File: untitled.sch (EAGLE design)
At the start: 62 parts, among them IC1 SIM900, IC2 ST1S10PHR, IC3 SMF05C, IC5 BQ24072, IC6 SIM68R, X1 ST-SMB-H, X2 ST-SMB-H

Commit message: Trace changes
Following items are changed:
- area between SIM900R and SIM68R footprints is restricted for placing
traces;
- some small changes in polygons around SIM900R;
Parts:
- removed R11: 22, rcl:R-EU_R0805
- removed SIM1: 912283001, con-molex-sim:912283001
- added JP10, JP11, JP12: (no value), pinhead:PINHD-1X1
- added SIM2: ICA-501, ICA-501:ICA-501
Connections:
- removed net N$15: IC3.5, R11.1, SIM1.PRESENCE
- net +4.8V: now also JP12.1
- net GND: now also SIM2.GND; no longer SIM1.GND
- net N$14: now also SIM2.RST; no longer SIM1.RST
- net N$17: now also SIM2.I/O; no longer SIM1.I/O
- net N$18: now also SIM2.CLK; no longer SIM1.CLK
- net SIM_PRESENCE: no longer R11.2
- net SIM_VDD: now also SIM2.VCC; no longer SIM1.VCC
- net VBAT: now also JP10.1, JP11.1
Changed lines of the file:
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@@
 <?xml version="1.0" encoding="utf-8"?>
 <!DOCTYPE eagle SYSTEM "eagle.dtd">
-<eagle version="6.4">
+<eagle version="6.5.0">
 <drawing>
 <settings>
@@
 <setting verticaltext="up"/>
 </settings>
-<grid distance="0.01" unitdist="inch" unit="inch" style="lines" multiple="1" display="no" altdistance="0.01" altunitdist="inch" altunit="inch"/>
+<grid distance="0.1" unitdist="inch" unit="inch" style="lines" multiple="1" display="no" altdistance="0.01" altunitdist="inch" altunit="inch"/>
 <layers>
 <layer number="1" name="Top" color="4" fill="1" visible="no" active="no"/>
@@
 <part name="R13" library="rcl" deviceset="R-EU_" device="R0805" value="22"/>
 <part name="R14" library="rcl" deviceset="R-EU_" device="R0805" value="22"/>
-<part name="R11" library="rcl" deviceset="R-EU_" device="R0805" value="22"/>
 <part name="VT3" library="transistor-npn" deviceset="MMBT3904" device=""/>
 <part name="GND24" library="supply1" deviceset="GND" device=""/>
@@
 <part name="R23" library="rcl" deviceset="R-EU_" device="R0805" value="4.7k"/>
 <part name="LED4" library="LED0805" deviceset="LED0805" device=""/>
-<part name="SIM1" library="con-molex-sim" deviceset="912283001" device=""/>
 <part name="IC6" library="sim68" deviceset="SIM68R" device=""/>
 <part name="SV2" library="con-lstb" deviceset="MA04-1" device=""/>
@@
 <part name="X2" library="coaxCon" deviceset="ST-SMB-H" device=""/>
 <part name="X1" library="coaxCon" deviceset="ST-SMB-H" device=""/>
+<part name="JP10" library="pinhead" deviceset="PINHD-1X1" device=""/>
+<part name="JP11" library="pinhead" deviceset="PINHD-1X1" device=""/>
+<part name="SIM2" library="ICA-501" deviceset="ICA-501" device=""/>
+<part name="JP12" library="pinhead" deviceset="PINHD-1X1" device=""/>
 </parts>
 <sheets>
@@
 <instance part="R13" gate="G$1" x="6.35" y="-48.26" rot="R180"/>
 <instance part="R14" gate="G$1" x="58.42" y="-48.26" rot="R180"/>
-<instance part="R11" gate="G$1" x="6.35" y="-50.8" rot="R180"/>
 <instance part="VT3" gate="G$1" x="29.21" y="85.09"/>
 <instance part="GND24" gate="1" x="31.75" y="72.39"/>
@@
 <instance part="R23" gate="G$1" x="-44.45" y="92.71" rot="R180"/>
 <instance part="LED4" gate="G$1" x="-29.21" y="101.6"/>
-<instance part="SIM1" gate="G$1" x="35.56" y="-48.26"/>
 <instance part="IC6" gate="G$1" x="-157.48" y="-58.42"/>
 <instance part="SV2" gate="1" x="-38.1" y="-35.56"/>
@@
 <instance part="X2" gate="G1" x="-136.398" y="-80.01" rot="R90"/>
 <instance part="X1" gate="G1" x="-10.414" y="76.962" rot="R270"/>
+<instance part="JP10" gate="G$1" x="-50.8" y="-71.12"/>
+<instance part="JP11" gate="G$1" x="-50.8" y="-81.28"/>
+<instance part="SIM2" gate="G$1" x="38.1" y="-45.72"/>
+<instance part="JP12" gate="G$1" x="-50.8" y="-91.44"/>
 </instances>
 <busses>
@@
 <pinref part="GND21" gate="1" pin="GND"/>
 <wire x1="53.34" y1="-43.18" x2="64.77" y2="-43.18" width="0.1524" layer="91"/>
-<pinref part="SIM1" gate="G$1" pin="GND"/>
+<pinref part="SIM2" gate="G$1" pin="GND"/>
 </segment>
 <segment>
@@
 <pinref part="IC5" gate="G$1" pin="IN"/>
 <pinref part="C5" gate="G$1" pin="1"/>
+</segment>
+<segment>
+<pinref part="JP12" gate="G$1" pin="1"/>
+<wire x1="-53.34" y1="-91.44" x2="-63.5" y2="-91.44" width="0.1524" layer="91"/>
+<label x="-63.5" y="-91.44" size="1.778" layer="95" rot="R180" xref="yes"/>
 </segment>
 </net>
@@
 <label x="-29.21" y="110.49" size="1.778" layer="95" rot="R180" xref="yes"/>
 </segment>
+<segment>
+<pinref part="JP10" gate="G$1" pin="1"/>
+<wire x1="-53.34" y1="-71.12" x2="-63.5" y2="-71.12" width="0.1524" layer="91"/>
+<label x="-63.5" y="-71.12" size="1.778" layer="95" rot="R180" xref="yes"/>
+</segment>
+<segment>
+<pinref part="JP11" gate="G$1" pin="1"/>
+<wire x1="-53.34" y1="-81.28" x2="-63.5" y2="-81.28" width="0.1524" layer="91"/>
+<label x="-63.5" y="-81.28" size="1.778" layer="95" rot="R180" xref="yes"/>
+</segment>
 </net>
 <net name="N$5" class="0">
@@
 <wire x1="5.08" y1="-43.18" x2="12.7" y2="-43.18" width="0.1524" layer="91"/>
 <junction x="12.7" y="-43.18"/>
-<wire x1="12.7" y1="-43.18" x2="17.78" y2="-43.18" width="0.1524" layer="91"/>
+<wire x1="12.7" y1="-43.18" x2="22.86" y2="-43.18" width="0.1524" layer="91"/>
 <wire x1="12.7" y1="-43.18" x2="12.7" y2="-62.23" width="0.1524" layer="91"/>
 <pinref part="IC3" gate="G$1" pin="1"/>
 <wire x1="12.7" y1="-62.23" x2="19.05" y2="-62.23" width="0.1524" layer="91"/>
 <wire x1="19.05" y1="-62.23" x2="19.05" y2="-63.5" width="0.1524" layer="91"/>
-<pinref part="SIM1" gate="G$1" pin="VCC"/>
+<pinref part="SIM2" gate="G$1" pin="VCC"/>
 </segment>
 <segment>
@@
 <wire x1="11.43" y1="-45.72" x2="13.97" y2="-45.72" width="0.1524" layer="91"/>
 <junction x="13.97" y="-45.72"/>
-<wire x1="13.97" y1="-45.72" x2="17.78" y2="-45.72" width="0.1524" layer="91"/>
+<wire x1="13.97" y1="-45.72" x2="22.86" y2="-45.72" width="0.1524" layer="91"/>
 <wire x1="13.97" y1="-45.72" x2="13.97" y2="-59.69" width="0.1524" layer="91"/>
 <pinref part="IC3" gate="G$1" pin="3"/>
 <wire x1="22.86" y1="-59.69" x2="22.86" y2="-63.5" width="0.1524" layer="91"/>
 <wire x1="13.97" y1="-59.69" x2="22.86" y2="-59.69" width="0.1524" layer="91"/>
-<pinref part="SIM1" gate="G$1" pin="RST"/>
+<pinref part="SIM2" gate="G$1" pin="RST"/>
 </segment>
 </net>
@@
 <wire x1="11.43" y1="-48.26" x2="15.24" y2="-48.26" width="0.1524" layer="91"/>
 <junction x="15.24" y="-48.26"/>
-<wire x1="15.24" y1="-48.26" x2="17.78" y2="-48.26" width="0.1524" layer="91"/>
+<wire x1="15.24" y1="-48.26" x2="22.86" y2="-48.26" width="0.1524" layer="91"/>
 <wire x1="15.24" y1="-48.26" x2="15.24" y2="-58.42" width="0.1524" layer="91"/>
 <pinref part="IC3" gate="G$1" pin="4"/>
 <wire x1="15.24" y1="-58.42" x2="26.67" y2="-58.42" width="0.1524" layer="91"/>
 <wire x1="26.67" y1="-58.42" x2="26.67" y2="-63.5" width="0.1524" layer="91"/>
-<pinref part="SIM1" gate="G$1" pin="CLK"/>
-</segment>
-</net>
-<net name="N$15" class="0">
-<segment>
-<wire x1="10.16" y1="-50.8" x2="11.43" y2="-50.8" width="0.1524" layer="91"/>
-<junction x="16.51" y="-50.8"/>
-<wire x1="11.43" y1="-50.8" x2="16.51" y2="-50.8" width="0.1524" layer="91"/>
-<wire x1="16.51" y1="-50.8" x2="17.78" y2="-50.8" width="0.1524" layer="91"/>
-<wire x1="16.51" y1="-50.8" x2="16.51" y2="-57.15" width="0.1524" layer="91"/>
-<pinref part="IC3" gate="G$1" pin="5"/>
-<wire x1="16.51" y1="-57.15" x2="30.48" y2="-57.15" width="0.1524" layer="91"/>
-<wire x1="30.48" y1="-57.15" x2="30.48" y2="-63.5" width="0.1524" layer="91"/>
-<pinref part="R11" gate="G$1" pin="1"/>
-<junction x="11.43" y="-50.8"/>
-<pinref part="SIM1" gate="G$1" pin="PRESENCE"/>
+<pinref part="SIM2" gate="G$1" pin="CLK"/>
 </segment>
 </net>
 <net name="SIM_PRESENCE" class="0">
-<segment>
-<pinref part="R11" gate="G$1" pin="2"/>
-<wire x1="1.27" y1="-50.8" x2="-1.27" y2="-50.8" width="0.1524" layer="91"/>
-<label x="-1.27" y="-50.8" size="1.778" layer="95" rot="R180" xref="yes"/>
-</segment>
 <segment>
 <pinref part="IC1" gate="G$1" pin="SIM_PRESENCE"/>
@@
 </segment>
 </net>
-<net name="N$17" class="0">
-<segment>
-<pinref part="R14" gate="G$1" pin="2"/>
-<pinref part="SIM1" gate="G$1" pin="I/O"/>
-</segment>
-</net>
 <net name="N$24" class="0">
 <segment>
@@
 </segment>
 </net>
+<net name="N$17" class="0">
+<segment>
+<pinref part="R14" gate="G$1" pin="2"/>
+<pinref part="SIM2" gate="G$1" pin="I/O"/>
+</segment>
+</net>

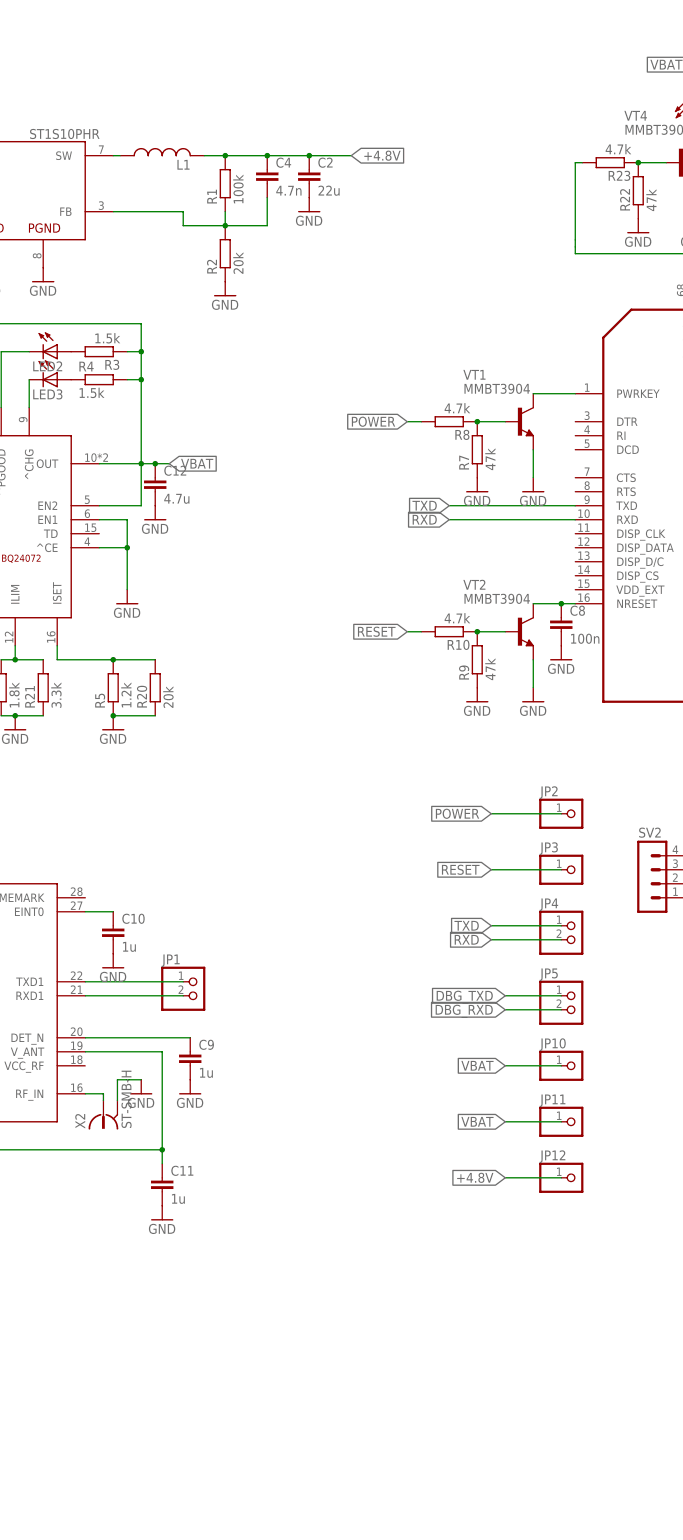
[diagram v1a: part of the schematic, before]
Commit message: ST1S10 layout
Supply component's location has been changed due to ST1S10 datasheet
layout considerations
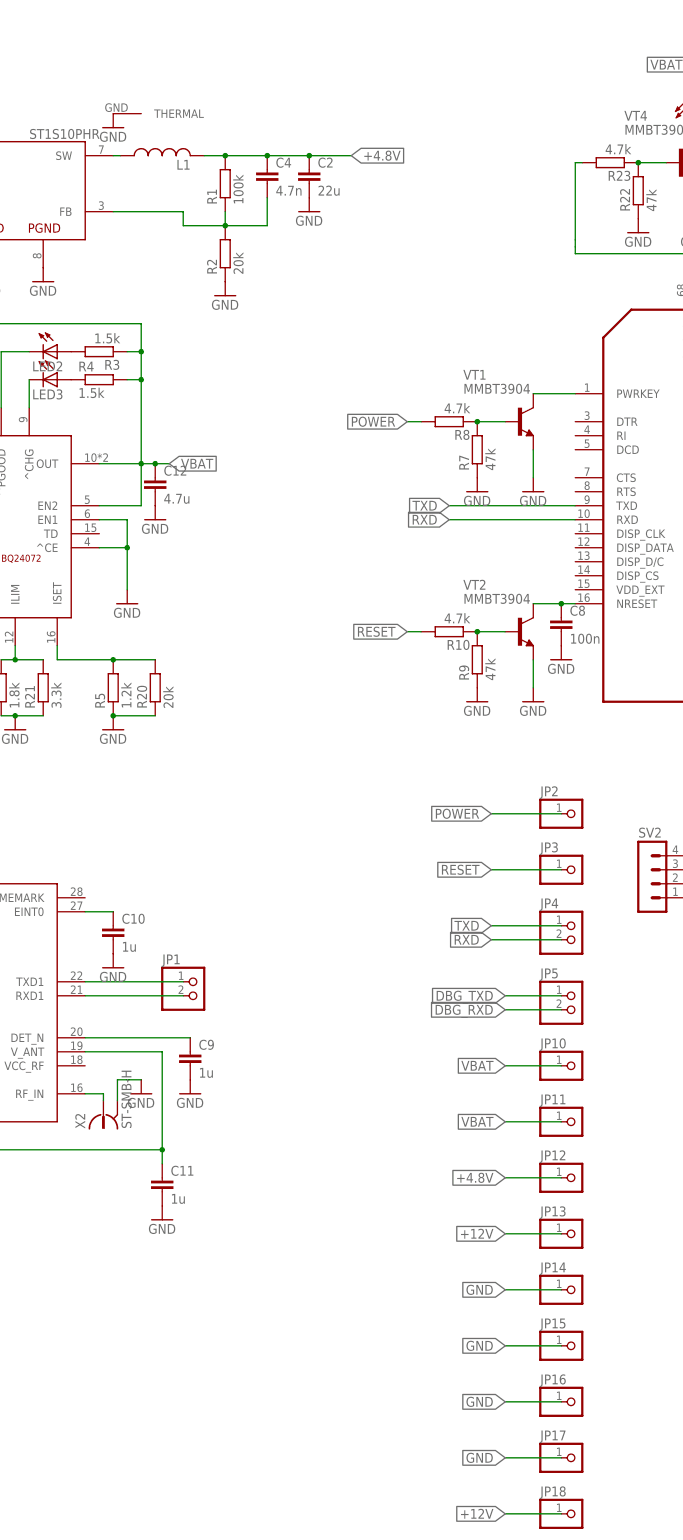
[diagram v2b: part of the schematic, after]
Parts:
- added JP13, JP14, JP15, JP16, JP17, JP18: (no value), pinhead:PINHD-1X1
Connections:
- net +12V: now also IC2G$1.EN, IC2G$1.VIN_A, IC2G$1.VIN_SW, JP13.1, JP18.1; no longer IC2.EN, IC2.VIN_A, IC2.VIN_SW
- net GND: now also IC2G$1.AGND, IC2G$1.PGND, IC2G$1.SYNC, IC2G$2.THERMAL, JP14.1, JP15.1, JP16.1, JP17.1; no longer IC2.AGND, IC2.PGND, IC2.SYNC
- net N$1: now also IC2G$1.SW; no longer IC2.SW
- net N$3: now also IC2G$1.FB; no longer IC2.FB
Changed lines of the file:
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@@
 <part name="SIM2" library="ICA-501" deviceset="ICA-501" device=""/>
 <part name="JP12" library="pinhead" deviceset="PINHD-1X1" device=""/>
+<part name="GND27" library="supply1" deviceset="GND" device=""/>
+<part name="JP13" library="pinhead" deviceset="PINHD-1X1" device=""/>
+<part name="JP14" library="pinhead" deviceset="PINHD-1X1" device=""/>
+<part name="JP15" library="pinhead" deviceset="PINHD-1X1" device=""/>
+<part name="JP16" library="pinhead" deviceset="PINHD-1X1" device=""/>
+<part name="JP17" library="pinhead" deviceset="PINHD-1X1" device=""/>
+<part name="JP18" library="pinhead" deviceset="PINHD-1X1" device=""/>
 </parts>
 <sheets>
@@
 <instance part="SIM2" gate="G$1" x="38.1" y="-45.72"/>
 <instance part="JP12" gate="G$1" x="-50.8" y="-91.44"/>
+<instance part="IC2" gate="G$2" x="-134.62" y="101.6" rot="R270"/>
+<instance part="GND27" gate="1" x="-134.62" y="99.06"/>
+<instance part="JP13" gate="G$1" x="-50.8" y="-101.6"/>
+<instance part="JP14" gate="G$1" x="-50.8" y="-111.76"/>
+<instance part="JP15" gate="G$1" x="-50.8" y="-121.92"/>
+<instance part="JP16" gate="G$1" x="-50.8" y="-132.08"/>
+<instance part="JP17" gate="G$1" x="-50.8" y="-142.24"/>
+<instance part="JP18" gate="G$1" x="-50.8" y="-152.4"/>
 </instances>
 <busses>
@@
 <wire x1="-12.954" y1="71.12" x2="-12.954" y2="74.422" width="0.1524" layer="91"/>
 </segment>
+<segment>
+<pinref part="IC2" gate="G$2" pin="THERMAL"/>
+<pinref part="GND27" gate="1" pin="GND"/>
+</segment>
+<segment>
+<pinref part="JP14" gate="G$1" pin="1"/>
+<wire x1="-53.34" y1="-111.76" x2="-63.5" y2="-111.76" width="0.1524" layer="91"/>
+<label x="-63.5" y="-111.76" size="1.778" layer="95" rot="R180" xref="yes"/>
+</segment>
+<segment>
+<pinref part="JP15" gate="G$1" pin="1"/>
+<wire x1="-53.34" y1="-121.92" x2="-63.5" y2="-121.92" width="0.1524" layer="91"/>
+<label x="-63.5" y="-121.92" size="1.778" layer="95" rot="R180" xref="yes"/>
+</segment>
+<segment>
+<pinref part="JP16" gate="G$1" pin="1"/>
+<wire x1="-53.34" y1="-132.08" x2="-63.5" y2="-132.08" width="0.1524" layer="91"/>
+<label x="-63.5" y="-132.08" size="1.778" layer="95" rot="R180" xref="yes"/>
+</segment>
+<segment>
+<pinref part="JP17" gate="G$1" pin="1"/>
+<wire x1="-53.34" y1="-142.24" x2="-63.5" y2="-142.24" width="0.1524" layer="91"/>
+<label x="-63.5" y="-142.24" size="1.778" layer="95" rot="R180" xref="yes"/>
+</segment>
 </net>
 <net name="+12V" class="0">
@@
 <wire x1="-198.12" y1="93.98" x2="-190.5" y2="93.98" width="0.1524" layer="91"/>
 </segment>
+<segment>
+<pinref part="JP13" gate="G$1" pin="1"/>
+<wire x1="-53.34" y1="-101.6" x2="-63.5" y2="-101.6" width="0.1524" layer="91"/>
+<label x="-63.5" y="-101.6" size="1.778" layer="95" rot="R180" xref="yes"/>
+</segment>
+<segment>
+<pinref part="JP18" gate="G$1" pin="1"/>
+<wire x1="-53.34" y1="-152.4" x2="-63.5" y2="-152.4" width="0.1524" layer="91"/>
+<label x="-63.5" y="-152.4" size="1.778" layer="95" rot="R180" xref="yes"/>
+</segment>
 </net>
